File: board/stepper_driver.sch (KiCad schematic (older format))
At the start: 12 parts

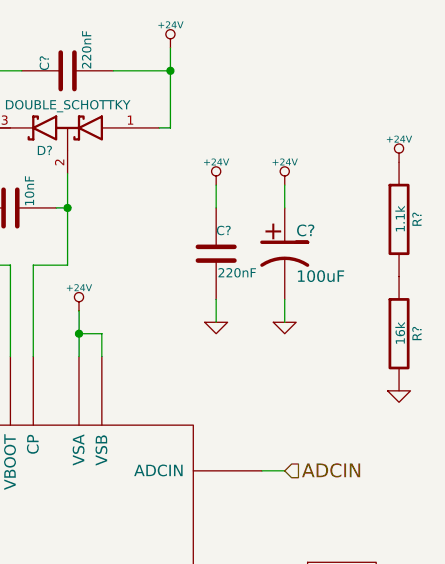
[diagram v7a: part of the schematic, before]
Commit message: Added 24V connector and fixed a few things on the 24V rail.
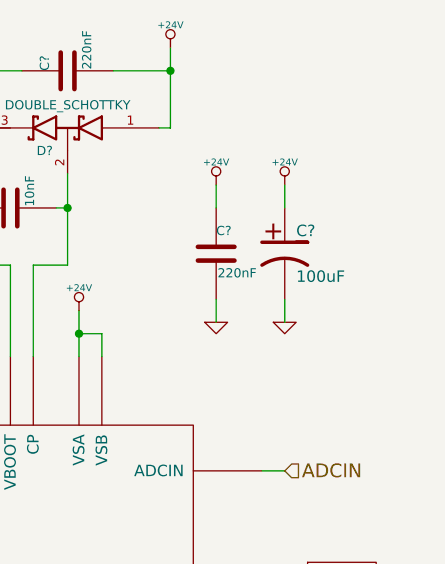
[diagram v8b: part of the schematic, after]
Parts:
- removed R?: 16k, symbol R
- removed R?: 1.1k, symbol R
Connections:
- new net: J?.~ (2B), U?.~ (~STBY/RST) (x3)
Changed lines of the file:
@@
 $Descr USLetter 11000 8500
 encoding utf-8
-Sheet 2 10
+Sheet 4 10
 Title "L64470 Stepper Driver"
 Date "21 jan 2014"
@@
 AR Path="/52E6C2E8/52E46BDA" Ref="J?"  Part="1"
 AR Path="/52E72F84/52E46BDA" Ref="J?"  Part="1"
+AR Path="/52EA366A/52E46BDA" Ref="J?"  Part="1"
 F 0 "J?" H 6800 4200 60  0000 C CNN
 F 1 "CONN_STEPPER" V 7150 4550 60  0001 C CNN
@@
 AR Path="/52E6C2E8/52E46C46" Ref="#PWR01"  Part="1"
 AR Path="/52E72F84/52E46C46" Ref="#PWR01"  Part="1"
+AR Path="/52EA366A/52E46C46" Ref="#PWR01"  Part="1"
 F 0 "#PWR01" H 4450 3200 30  0001 C CNN
 F 1 "GND" H 4450 3130 30  0001 C CNN
@@
 AR Path="/52E6C2E8/52E46C5A" Ref="#PWR02"  Part="1"
 AR Path="/52E72F84/52E46C5A" Ref="#PWR02"  Part="1"
+AR Path="/52EA366A/52E46C5A" Ref="#PWR02"  Part="1"
 F 0 "#PWR02" H 4750 3200 30  0001 C CNN
 F 1 "GND" H 4750 3130 30  0001 C CNN
@@
 AR Path="/52E6C2E8/52E46C96" Ref="#PWR03"  Part="1"
 AR Path="/52E72F84/52E46C96" Ref="#PWR03"  Part="1"
+AR Path="/52EA366A/52E46C96" Ref="#PWR03"  Part="1"
 F 0 "#PWR03" H 4450 2560 30  0001 C CNN
 F 1 "+3.3V" H 4450 2710 30  0000 C CNN
@@
 AR Path="/52E6C2E8/52E46CA8" Ref="#PWR04"  Part="1"
 AR Path="/52E72F84/52E46CA8" Ref="#PWR04"  Part="1"
+AR Path="/52EA366A/52E46CA8" Ref="#PWR04"  Part="1"
 F 0 "#PWR04" H 4750 2560 30  0001 C CNN
 F 1 "+3.3V" H 4750 2710 30  0000 C CNN
@@
 AR Path="/52E6C2E8/52E46CC8" Ref="#PWR05"  Part="1"
 AR Path="/52E72F84/52E46CC8" Ref="#PWR05"  Part="1"
+AR Path="/52EA366A/52E46CC8" Ref="#PWR05"  Part="1"
 F 0 "#PWR05" H 5150 3110 30  0001 C CNN
 F 1 "+3.3V" H 5150 3260 30  0000 C CNN
@@
 AR Path="/52E6C2E8/52E46D7E" Ref="#PWR06"  Part="1"
 AR Path="/52E72F84/52E46D7E" Ref="#PWR06"  Part="1"
+AR Path="/52EA366A/52E46D7E" Ref="#PWR06"  Part="1"
 F 0 "#PWR06" H 5750 3100 20  0001 C CNN
 F 1 "+24V" H 5750 3250 30  0000 C CNN
@@
 AR Path="/52E6C2E8/52E46E92" Ref="#PWR07"  Part="1"
 AR Path="/52E72F84/52E46E92" Ref="#PWR07"  Part="1"
+AR Path="/52EA366A/52E46E92" Ref="#PWR07"  Part="1"
 F 0 "#PWR07" H 6150 1950 20  0001 C CNN
 F 1 "+24V" H 6150 2100 30  0000 C CNN
@@
 AR Path="/52E6C2E8/52E46FD2" Ref="#PWR08"  Part="1"
 AR Path="/52E72F84/52E46FD2" Ref="#PWR08"  Part="1"
+AR Path="/52EA366A/52E46FD2" Ref="#PWR08"  Part="1"
 F 0 "#PWR08" H 5450 5950 30  0001 C CNN
 F 1 "GND" H 5450 5880 30  0001 C CNN
@@
 AR Path="/52E6C2E8/52E47021" Ref="#PWR09"  Part="1"
 AR Path="/52E72F84/52E47021" Ref="#PWR09"  Part="1"
+AR Path="/52EA366A/52E47021" Ref="#PWR09"  Part="1"
 F 0 "#PWR09" H 6650 5350 30  0001 C CNN
 F 1 "GND" H 6650 5280 30  0001 C CNN
@@
 AR Path="/52E6C2E8/52E47051" Ref="#PWR010"  Part="1"
 AR Path="/52E72F84/52E47051" Ref="#PWR010"  Part="1"
+AR Path="/52EA366A/52E47051" Ref="#PWR010"  Part="1"
 F 0 "#PWR010" H 4450 5550 30  0001 C CNN
 F 1 "GND" H 4450 5480 30  0001 C CNN
@@
 AR Path="/52E6C2E8/52E4727D" Ref="P?"  Part="1"
 AR Path="/52E72F84/52E4727D" Ref="P?"  Part="1"
+AR Path="/52EA366A/52E4727D" Ref="P?"  Part="1"
 F 0 "P?" V 3950 5350 40  0000 C CNN
 F 1 "CONN_2" V 4050 5350 40  0000 C CNN
@@
 Wire Wire Line
 	5550 5850 5550 5750
-$Comp
-L R R?
-U 1 1 52E475E9
-P 7150 3250
-AR Path="/52E6C2E8/52E475E9" Ref="R?"  Part="1"
-AR Path="/52E72F84/52E475E9" Ref="R?"  Part="1"
-F 0 "R?" V 7230 3250 40  0000 C CNN
-F 1 "16k" V 7157 3251 40  0000 C CNN
-F 2 "" V 7080 3250 30  0000 C CNN
-F 3 "" H 7150 3250 30  0000 C CNN
-	1    7150 3250
-	1    0    0    -1
-$EndComp
-$Comp
-L GND #PWR011
-U 1 1 52E475F4
-P 7150 3500
-AR Path="/52E6C2E8/52E475F4" Ref="#PWR011"  Part="1"
-AR Path="/52E72F84/52E475F4" Ref="#PWR011"  Part="1"
-F 0 "#PWR011" H 7150 3500 30  0001 C CNN
-F 1 "GND" H 7150 3430 30  0001 C CNN
-F 2 "" H 7150 3500 60  0000 C CNN
-F 3 "" H 7150 3500 60  0000 C CNN
-	1    7150 3500
-	1    0    0    -1
-$EndComp
-$Comp
-L +24V #PWR012
-U 1 1 52E47672
-P 7150 2500
-AR Path="/52E6C2E8/52E47672" Ref="#PWR012"  Part="1"
-AR Path="/52E72F84/52E47672" Ref="#PWR012"  Part="1"
-F 0 "#PWR012" H 7150 2450 20  0001 C CNN
-F 1 "+24V" H 7150 2600 30  0000 C CNN
-F 2 "" H 7150 2500 60  0000 C CNN
-F 3 "" H 7150 2500 60  0000 C CNN
-	1    7150 2500
-	1    0    0    -1
-$EndComp
-$Comp
-L R R?
-U 1 1 52E47703
-P 7150 2750
-AR Path="/52E6C2E8/52E47703" Ref="R?"  Part="1"
-AR Path="/52E72F84/52E47703" Ref="R?"  Part="1"
-F 0 "R?" V 7230 2750 40  0000 C CNN
-F 1 "1.1k" V 7157 2751 40  0000 C CNN
-F 2 "" V 7080 2750 30  0000 C CNN
-F 3 "" H 7150 2750 30  0000 C CNN
-	1    7150 2750
-	1    0    0    -1
-$EndComp
 Text HLabel 6650 3850 2    60   Input ~ 0
 ADCIN
@@
 AR Path="/52E6C2E8/52E477BA" Ref="#PWR013"  Part="1"
 AR Path="/52E72F84/52E477BA" Ref="#PWR013"  Part="1"
+AR Path="/52EA366A/52E477BA" Ref="#PWR013"  Part="1"
 F 0 "#PWR013" H 6350 3200 30  0001 C CNN
 F 1 "GND" H 6350 3130 30  0001 C CNN
@@
 AR Path="/52E6C2E8/52E477C5" Ref="#PWR014"  Part="1"
 AR Path="/52E72F84/52E477C5" Ref="#PWR014"  Part="1"
+AR Path="/52EA366A/52E477C5" Ref="#PWR014"  Part="1"
 F 0 "#PWR014" H 6650 3200 30  0001 C CNN
 F 1 "GND" H 6650 3130 30  0001 C CNN
@@
 AR Path="/52E6C2E8/52E477D0" Ref="#PWR015"  Part="1"
 AR Path="/52E72F84/52E477D0" Ref="#PWR015"  Part="1"
+AR Path="/52EA366A/52E477D0" Ref="#PWR015"  Part="1"
 F 0 "#PWR015" H 6350 2550 20  0001 C CNN
 F 1 "+24V" H 6350 2700 30  0000 C CNN
@@
 AR Path="/52E6C2E8/52E477DB" Ref="#PWR016"  Part="1"
 AR Path="/52E72F84/52E477DB" Ref="#PWR016"  Part="1"
+AR Path="/52EA366A/52E477DB" Ref="#PWR016"  Part="1"
 F 0 "#PWR016" H 6650 2550 20  0001 C CNN
 F 1 "+24V" H 6650 2700 30  0000 C CNN
@@
 AR Path="/52E6C2E8/52E4789D" Ref="C?"  Part="1"
 AR Path="/52E72F84/52E4789D" Ref="C?"  Part="1"
+AR Path="/52EA366A/52E4789D" Ref="C?"  Part="1"
 F 0 "C?" H 4450 3000 40  0000 L CNN
 F 1 "100nF" H 4456 2815 40  0000 L CNN
@@
 AR Path="/52E6C2E8/52E478B3" Ref="C?"  Part="1"
 AR Path="/52E72F84/52E478B3" Ref="C?"  Part="1"
+AR Path="/52EA366A/52E478B3" Ref="C?"  Part="1"
 F 0 "C?" H 6350 3000 40  0000 L CNN
 F 1 "220nF" H 6356 2815 40  0000 L CNN
@@
 AR Path="/52E6C2E8/52E478C4" Ref="C?"  Part="1"
 AR Path="/52E72F84/52E478C4" Ref="C?"  Part="1"
+AR Path="/52EA366A/52E478C4" Ref="C?"  Part="1"
 F 0 "C?" H 6700 3000 50  0000 L CNN
 F 1 "100uF" H 6700 2800 50  0000 L CNN
@@
 AR Path="/52E6C2E8/52E47A96" Ref="C?"  Part="1"
 AR Path="/52E72F84/52E47A96" Ref="C?"  Part="1"
+AR Path="/52EA366A/52E47A96" Ref="C?"  Part="1"
 F 0 "C?" H 4800 3000 50  0000 L CNN
 F 1 "10uF" H 4800 2800 50  0000 L CNN
@@
 AR Path="/52E6C2E8/52E47AD8" Ref="C?"  Part="1"
 AR Path="/52E72F84/52E47AD8" Ref="C?"  Part="1"
+AR Path="/52EA366A/52E47AD8" Ref="C?"  Part="1"
 F 0 "C?" H 5700 2200 40  0000 L CNN
 F 1 "220nF" H 5706 2015 40  0000 L CNN
@@
 AR Path="/52E6C2E8/52E47AE3" Ref="C?"  Part="1"
 AR Path="/52E72F84/52E47AE3" Ref="C?"  Part="1"
+AR Path="/52EA366A/52E47AE3" Ref="C?"  Part="1"
 F 0 "C?" H 5450 2800 40  0000 L CNN
 F 1 "10nF" H 5456 2615 40  0000 L CNN
@@
 AR Path="/52E6C2E8/52E6B5EE" Ref="U?"  Part="1"
 AR Path="/52E72F84/52E6B5EE" Ref="U?"  Part="1"
+AR Path="/52EA366A/52E6B5EE" Ref="U?"  Part="1"
 F 0 "U?" H 4850 3600 60  0000 C CNN
 F 1 "L6470" H 5500 4550 60  0000 C CNN
@@
 U 1 1 52F6EE9F
 P 5700 2350
+AR Path="/52E6C2E8/52F6EE9F" Ref="D?"  Part="1"
+AR Path="/52EA366A/52F6EE9F" Ref="D?"  Part="1"
 F 0 "D?" H 5800 2250 40  0000 C CNN
 F 1 "DOUBLE_SCHOTTKY" H 5700 2450 40  0000 C CNN
